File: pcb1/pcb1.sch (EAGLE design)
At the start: 29 parts, among them J1 12V, J2 24V, J3 RTD, J4 SPT25, J5 SPT25, J6 SPDT25, J7 TMP006, J8 VN-200, Q1 SI01P10-TP, Q2 SI01P10-TP

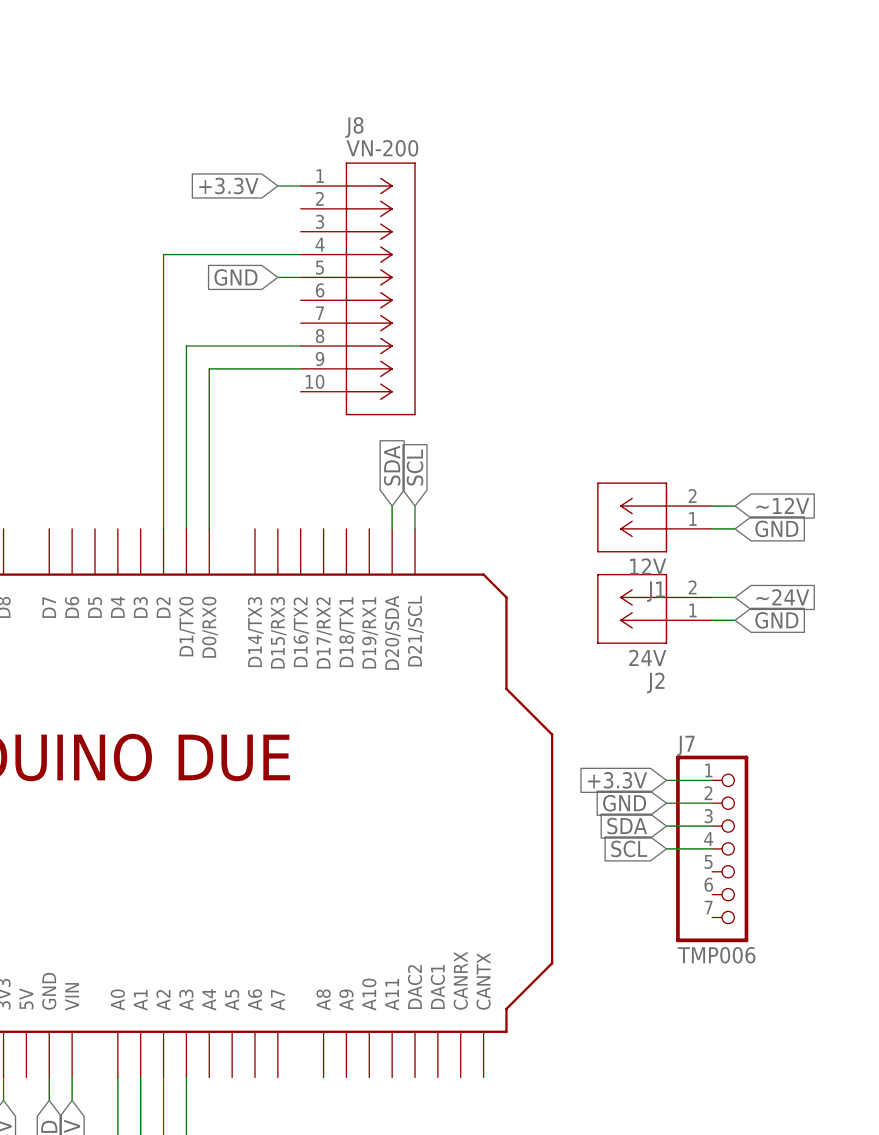
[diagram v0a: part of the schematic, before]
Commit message: Changed TMP006 Connection
* changed tmp006 connection to molex 4pin
+ Added SDA/SCL pullup resistors
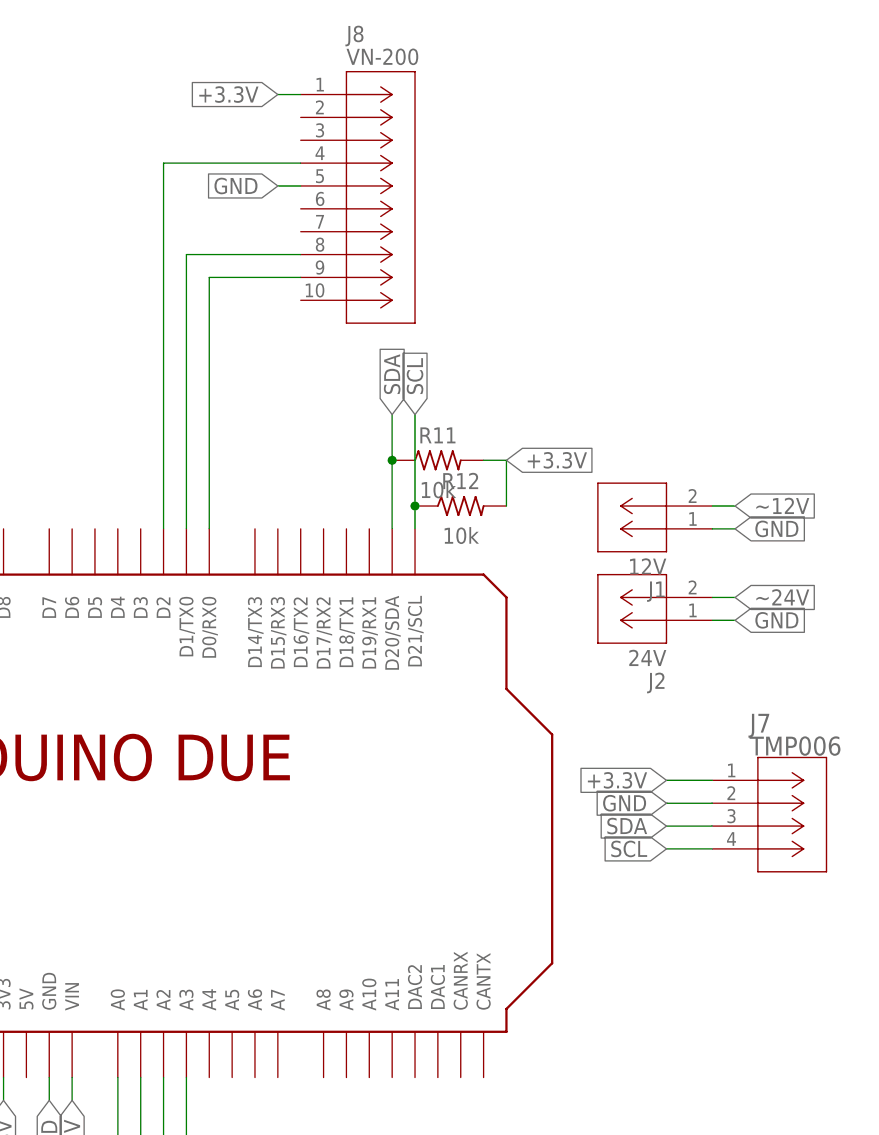
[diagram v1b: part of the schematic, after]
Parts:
- added R11, R12: 10k, Resistor:R-US_CHIP-0603(1608-METRIC)
- J7: device Female Pin Headers:HEADER_FEMALE_7 -> Molex Micro-Lock PLUS:MICROLOCK-4PIN
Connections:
- net +3.3V: now also R11.2, R12.2
- net SCL: now also R12.1
- net SDA: now also R11.1
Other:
- moved on the sheet: J8
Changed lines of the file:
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@@
 <part name="F1" library="Circuit-Protection" deviceset="FUSE" device="CHIP-0603(1608-METRIC)" package3d_urn="urn:adsk.eagle:package:16378156/1" technology="_" value="1A"/>
 <part name="F2" library="Circuit-Protection" deviceset="FUSE" device="CHIP-0603(1608-METRIC)" package3d_urn="urn:adsk.eagle:package:16378156/1" technology="_" value="1A"/>
-<part name="J7" library="Female Pin Headers" library_urn="urn:adsk.wipprod:fs.file:vf.ChRTMJm5T8S79gGQJfnxFg" deviceset="HEADER_FEMALE_7" device="" package3d_urn="urn:adsk.wipprod:fs.file:vf.c9GOuMoXQyiwz8Kh6BO9EQ?version=2" value="TMP006"/>
 <part name="J1" library="Molex Micro-Lock PLUS" library_urn="urn:adsk.wipprod:fs.file:vf.7BFQp9fYT0myC-vL_u_pew" deviceset="MICROLOCK-2PIN" device="CON_5055670271" package3d_urn="urn:adsk.wipprod:fs.file:vf.DbgxurRFTwKL72n502snIg?version=2" value="12V"/>
 <part name="J2" library="Molex Micro-Lock PLUS" library_urn="urn:adsk.wipprod:fs.file:vf.7BFQp9fYT0myC-vL_u_pew" deviceset="MICROLOCK-2PIN" device="CON_5055670271" package3d_urn="urn:adsk.wipprod:fs.file:vf.DbgxurRFTwKL72n502snIg?version=2" value="24V"/>
@@
 <part name="R9" library="Resistor" deviceset="R-US" device="CHIP-0603(1608-METRIC)" package3d_urn="urn:adsk.eagle:package:16378565/2" technology="_" value="15"/>
 <part name="R10" library="Resistor" deviceset="R-US" device="CHIP-0603(1608-METRIC)" package3d_urn="urn:adsk.eagle:package:16378565/2" technology="_" value="15"/>
+<part name="J7" library="Molex Micro-Lock PLUS" library_urn="urn:adsk.wipprod:fs.file:vf.aLnYsiJBRyGIcsa2SAseLA" deviceset="MICROLOCK-4PIN" device="" package3d_urn="urn:adsk.wipprod:fs.file:vf.qgFO0TMcQe-EH4rWbP_Pug?version=2" value="TMP006"/>
+<part name="R11" library="Resistor" deviceset="R-US" device="CHIP-0603(1608-METRIC)" package3d_urn="urn:adsk.eagle:package:16378565/2" technology="_" value="10k"/>
+<part name="R12" library="Resistor" deviceset="R-US" device="CHIP-0603(1608-METRIC)" package3d_urn="urn:adsk.eagle:package:16378565/2" technology="_" value="10k"/>
 </parts>
 <sheets>
@@
 <attribute name="VALUE" x="-118.11" y="-30.861" size="1.778" layer="96"/>
 </instance>
-<instance part="J7" gate="G$1" x="53.34" y="-12.7" smashed="yes">
-<attribute name="NAME" x="46.99" y="-1.905" size="1.778" layer="95"/>
-<attribute name="VALUE" x="46.99" y="-25.4" size="1.778" layer="96"/>
-</instance>
 <instance part="J1" gate="G$1" x="50.8" y="22.86" smashed="yes" rot="R180">
 <attribute name="NAME" x="45.72" y="17.018" size="1.778" layer="95" rot="R180"/>
@@
 <attribute name="VALUE" x="45.72" y="9.398" size="1.778" layer="96" rot="R180"/>
 </instance>
-<instance part="J8" gate="G$1" x="5.08" y="60.96" smashed="yes">
-<attribute name="NAME" x="10.16" y="66.802" size="1.778" layer="95"/>
-<attribute name="VALUE" x="10.16" y="64.262" size="1.778" layer="96"/>
+<instance part="J8" gate="G$1" x="5.08" y="71.12" smashed="yes">
+<attribute name="NAME" x="10.16" y="76.962" size="1.778" layer="95"/>
+<attribute name="VALUE" x="10.16" y="74.422" size="1.778" layer="96"/>
 </instance>
 <instance part="J3" gate="G$1" x="12.7" y="-55.88" smashed="yes">
@@
 <attribute name="NAME" x="-22.86" y="-70.8914" size="1.778" layer="95" align="center"/>
 <attribute name="VALUE" x="-22.86" y="-76.962" size="1.778" layer="96" align="center"/>
+</instance>
+<instance part="J7" gate="G$1" x="50.8" y="-5.08" smashed="yes">
+<attribute name="NAME" x="54.9646" y="0.2286" size="2.083" layer="95" ratio="6"/>
+<attribute name="VALUE" x="54.9646" y="-2.3114" size="2.083" layer="96" ratio="6"/>
+</instance>
+<instance part="R11" gate="G$1" x="20.32" y="30.48" smashed="yes">
+<attribute name="NAME" x="20.32" y="33.2486" size="1.778" layer="95" align="center"/>
+<attribute name="VALUE" x="20.32" y="27.178" size="1.778" layer="96" align="center"/>
+</instance>
+<instance part="R12" gate="G$1" x="22.86" y="25.4" smashed="yes">
+<attribute name="NAME" x="22.86" y="28.1686" size="1.778" layer="95" align="center"/>
+<attribute name="VALUE" x="22.86" y="22.098" size="1.778" layer="96" align="center"/>
 </instance>
 </instances>
@@
 </segment>
 <segment>
-<wire x1="5.08" y1="50.8" x2="2.54" y2="50.8" width="0.1524" layer="91"/>
-<label x="2.54" y="50.8" size="1.778" layer="95" rot="R180" xref="yes"/>
+<wire x1="5.08" y1="60.96" x2="2.54" y2="60.96" width="0.1524" layer="91"/>
+<label x="2.54" y="60.96" size="1.778" layer="95" rot="R180" xref="yes"/>
 <pinref part="J8" gate="G$1" pin="6"/>
 </segment>
@@
 <net name="N$5" class="0">
 <segment>
-<wire x1="5.08" y1="40.64" x2="-5.08" y2="40.64" width="0.1524" layer="91"/>
-<wire x1="-5.08" y1="40.64" x2="-5.08" y2="22.86" width="0.1524" layer="91"/>
+<wire x1="5.08" y1="50.8" x2="-5.08" y2="50.8" width="0.1524" layer="91"/>
+<wire x1="-5.08" y1="50.8" x2="-5.08" y2="22.86" width="0.1524" layer="91"/>
 <pinref part="U$1" gate="G$1" pin="D0/RX0"/>
 <pinref part="J8" gate="G$1" pin="10"/>
@@
 <net name="N$6" class="0">
 <segment>
-<wire x1="5.08" y1="43.18" x2="-7.62" y2="43.18" width="0.1524" layer="91"/>
-<wire x1="-7.62" y1="43.18" x2="-7.62" y2="22.86" width="0.1524" layer="91"/>
+<wire x1="5.08" y1="53.34" x2="-7.62" y2="53.34" width="0.1524" layer="91"/>
+<wire x1="-7.62" y1="53.34" x2="-7.62" y2="22.86" width="0.1524" layer="91"/>
 <pinref part="U$1" gate="G$1" pin="D1/TX0"/>
 <pinref part="J8" gate="G$1" pin="9"/>
@@
 <net name="N$7" class="0">
 <segment>
-<wire x1="5.08" y1="53.34" x2="-10.16" y2="53.34" width="0.1524" layer="91"/>
-<wire x1="-10.16" y1="53.34" x2="-10.16" y2="22.86" width="0.1524" layer="91"/>
+<wire x1="5.08" y1="63.5" x2="-10.16" y2="63.5" width="0.1524" layer="91"/>
+<wire x1="-10.16" y1="63.5" x2="-10.16" y2="22.86" width="0.1524" layer="91"/>
 <pinref part="U$1" gate="G$1" pin="D2"/>
 <pinref part="J8" gate="G$1" pin="5"/>
@@
 <segment>
 <pinref part="U$1" gate="G$1" pin="D20/SDA"/>
-<wire x1="15.24" y1="22.86" x2="15.24" y2="25.4" width="0.1524" layer="91"/>
-<label x="15.24" y="25.4" size="1.778" layer="95" rot="R90" xref="yes"/>
+<wire x1="15.24" y1="22.86" x2="15.24" y2="30.48" width="0.1524" layer="91"/>
+<label x="15.24" y="35.56" size="1.778" layer="95" rot="R90" xref="yes"/>
+<pinref part="R11" gate="G$1" pin="1"/>
+<wire x1="15.24" y1="30.48" x2="15.24" y2="35.56" width="0.1524" layer="91"/>
+<junction x="15.24" y="30.48"/>
 </segment>
 </net>
@@
 <pinref part="U$1" gate="G$1" pin="D21/SCL"/>
 <wire x1="17.78" y1="22.86" x2="17.78" y2="25.4" width="0.1524" layer="91"/>
-<label x="17.78" y="25.4" size="1.778" layer="95" rot="R90" xref="yes"/>
+<label x="17.78" y="35.56" size="1.778" layer="95" rot="R90" xref="yes"/>
+<pinref part="R12" gate="G$1" pin="1"/>
+<wire x1="17.78" y1="25.4" x2="17.78" y2="35.56" width="0.1524" layer="91"/>
+<junction x="17.78" y="25.4"/>
 </segment>
 </net>
 <net name="+3.3V" class="0">
 <segment>
-<wire x1="5.08" y1="60.96" x2="2.54" y2="60.96" width="0.1524" layer="91"/>
-<label x="2.54" y="60.96" size="1.778" layer="95" rot="R180" xref="yes"/>
+<wire x1="5.08" y1="71.12" x2="2.54" y2="71.12" width="0.1524" layer="91"/>
+<label x="2.54" y="71.12" size="1.778" layer="95" rot="R180" xref="yes"/>
 <pinref part="J8" gate="G$1" pin="2"/>
 </segment>
@@
 <pinref part="J7" gate="G$1" pin="1"/>
 </segment>
-</net>
+<segment>
+<pinref part="R11" gate="G$1" pin="2"/>
+<wire x1="25.4" y1="30.48" x2="27.94" y2="30.48" width="0.1524" layer="91"/>
+<wire x1="27.94" y1="30.48" x2="27.94" y2="25.4" width="0.1524" layer="91"/>
+<pinref part="R12" gate="G$1" pin="2"/>
+<label x="27.94" y="30.48" size="1.778" layer="95" xref="yes"/>
+</segment>
+</net>
